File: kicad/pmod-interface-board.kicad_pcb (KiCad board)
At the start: 4 copper layers, 83.8 x 61 mm, 30 parts, among them J1 PMOD Connector 1, J2 PMOD Connector 2, J4 Gameboy Cart Connector, U1 74HCT541, U2 74HCT541, U3 74HC595, U4 74HC595, U5 74HC595, U6 74HC597

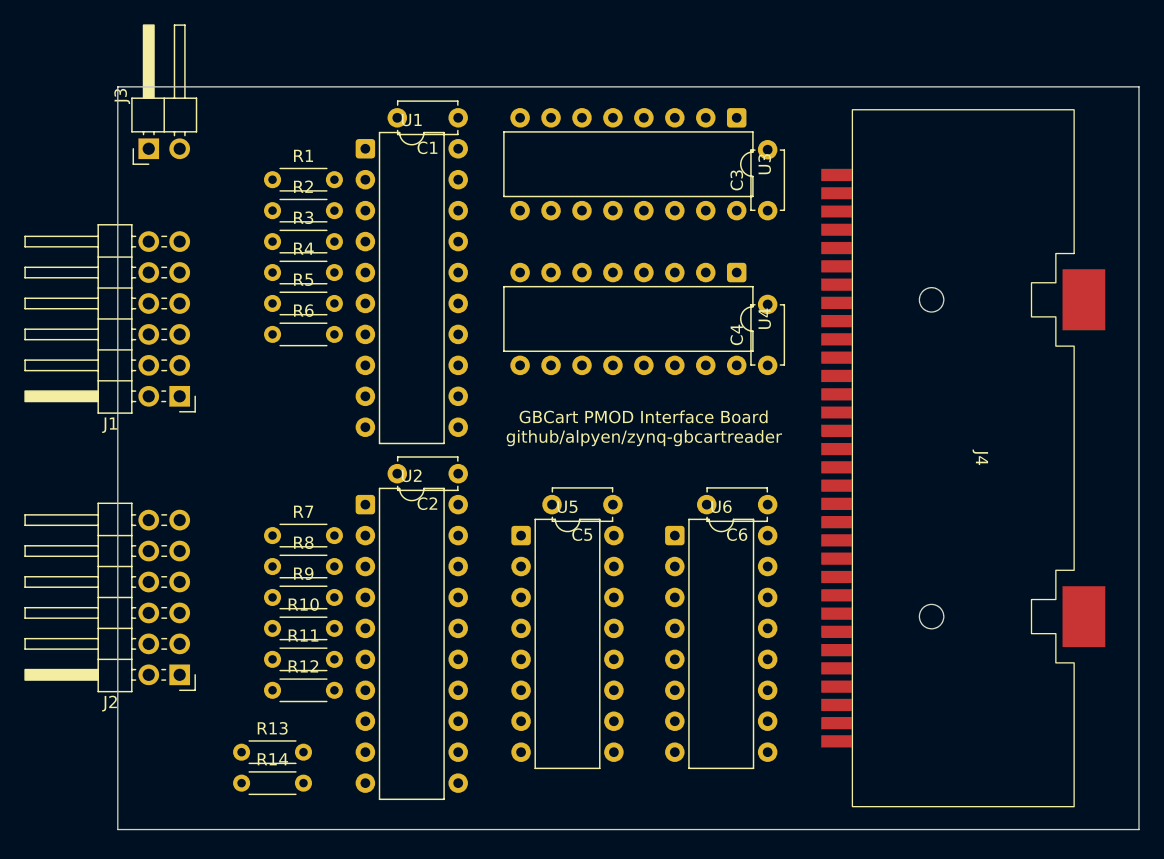
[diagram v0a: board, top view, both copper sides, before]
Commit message: kicad: routing completed, sped up resistor divider by lowering values
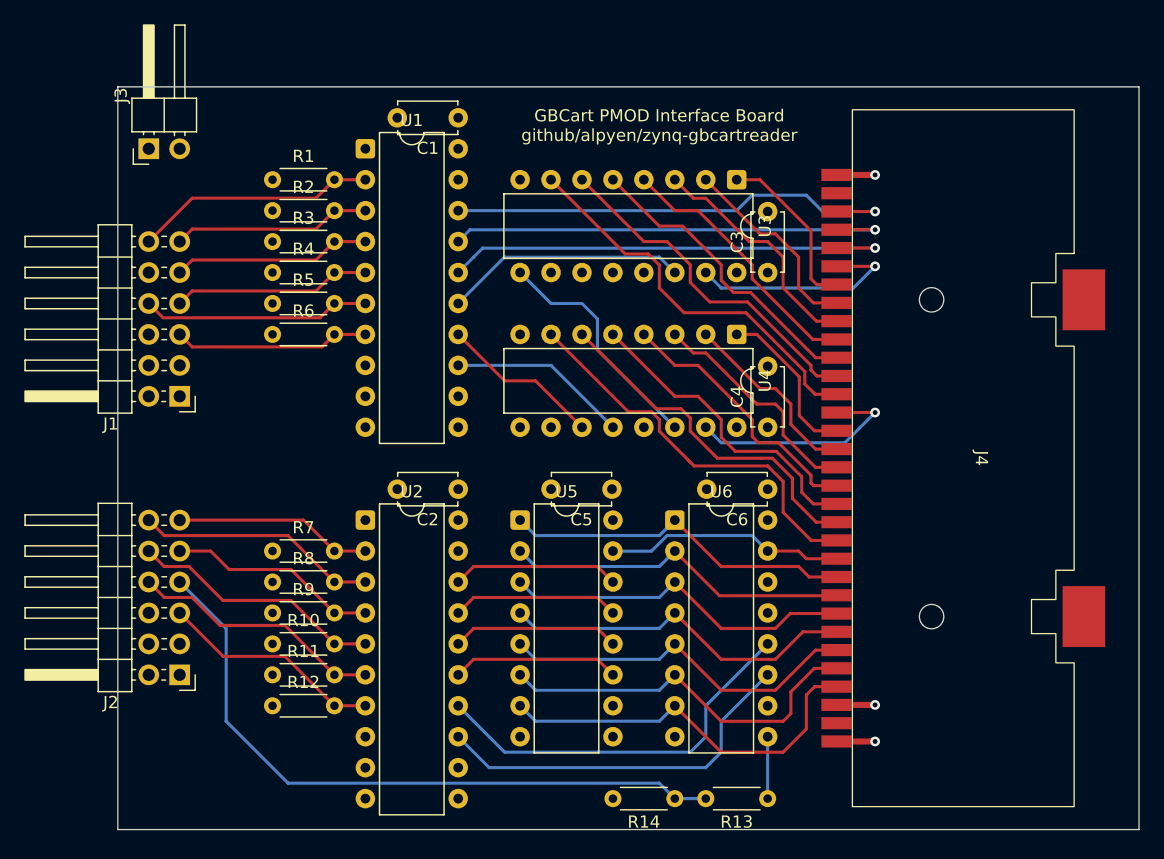
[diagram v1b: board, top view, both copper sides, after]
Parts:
- R13: value 510R -> 100R
- R14: value 1K -> 200R
- moved R13 43.3 mm to (162.6, 119.4), turned to 180 degrees
- moved R14 35.6 mm to (154.9, 119.4), turned to 180 degrees
- moved C4 5.08 mm to (162.6, 88.9)
- moved C3 5.08 mm to (162.6, 76.2)
- moved U3 5.08 mm to (160.0, 68.6)
- moved U4 5.08 mm to (160.0, 81.3)
- moved U5 1.27 mm to (142.2, 96.5)
- moved C5 1.27 mm to (149.8, 94.0)
- moved C2 1.27 mm to (137.2, 94.0)
- moved R10 1.27 mm to (121.9, 106.7)
- moved R12 1.27 mm to (121.9, 111.8)
- moved U6 1.27 mm to (154.9, 96.5)
- moved C6 1.27 mm to (162.6, 94.0)
- moved R11 1.27 mm to (121.9, 109.2)
- moved R7 1.27 mm to (121.9, 99.1)
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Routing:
- net DATA_IN_SDATA_out: track 0.00 -> 55.0 mm
- net /~{WR}: track 0.00 -> 38.5 mm, vias 0 -> 1
- net /~{CS}: track 0.00 -> 38.2 mm, vias 0 -> 1
- net /~{RD}: track 0.00 -> 37.8 mm, vias 0 -> 1
- net /A15: track 0.00 -> 32.7 mm
- net /D7: track 0.00 -> 32.5 mm
- net /A7: track 0.00 -> 32.4 mm
- net /DATA_IN_RCLK: track 0.00 -> 32.1 mm
- net /D6: track 0.00 -> 31.4 mm
- net /DATA_IN_SCLK: track 0.00 -> 31.1 mm
- net /D5: track 0.00 -> 30.0 mm
- net /D4: track 0.00 -> 29.5 mm
- net /D3: track 0.00 -> 29.1 mm
- net /D1: track 0.00 -> 29.0 mm
- net /A14: track 0.00 -> 28.9 mm
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- added copper zone on In2.Cu, net +5V
- added copper zone on In1.Cu, net GND

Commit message: kicad: switched out power header and moved pmod connectors closer
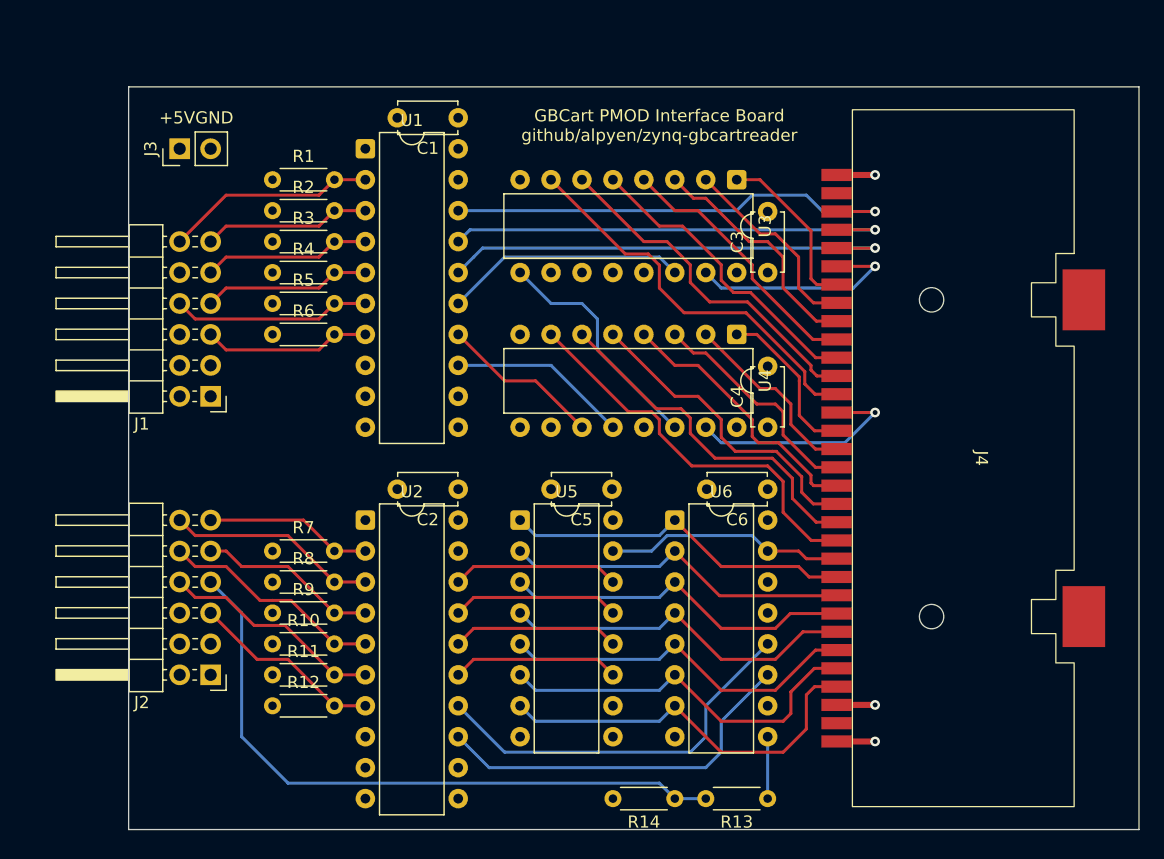
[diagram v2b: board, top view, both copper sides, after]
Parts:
- J3: footprint Connector_PinHeader_2.54mm:PinHeader_1x02_P2.54mm_Horizontal -> Connector_PinHeader_2.54mm:PinHeader_1x02_P2.54mm_Vertical
- moved J1 2.54 mm to (116.8, 86.4)
- moved J2 2.54 mm to (116.8, 109.2)
- moved J3 2.54 mm to (114.3, 66.0)
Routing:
- net DATA_IN_RCLK_in: track 21.4 -> 18.4 mm
- net ~{RD}_in: track 16.3 -> 13.8 mm
- net DATA_IN_SCLK_in: track 18.4 -> 15.9 mm
- net ~{CS}_in: track 16.3 -> 13.8 mm
- net DATA_OUT_SDATA_in: track 16.3 -> 13.8 mm
- net DATA_OUT_RCLK_in: track 17.3 -> 14.8 mm
- net ADDR_SDATA_in: track 16.3 -> 13.8 mm
- net ~{WR}_in: track 19.9 -> 17.3 mm
- net DATA_OUT_SCLK_in: track 20.9 -> 18.4 mm
- net DATA_OUT_OE_in: track 19.9 -> 17.3 mm
- net ADDR_SCLK_in: track 18.8 -> 16.3 mm
- net ADDR_RCLK_in: track 16.1 -> 13.8 mm
- net DATA_IN_SDATA_out: track 55.0 -> 54.0 mm
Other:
- board size 83.8 x 61 mm -> 82.9 x 61 mm
- board text added: "+5V"
- board text added: "GND"
